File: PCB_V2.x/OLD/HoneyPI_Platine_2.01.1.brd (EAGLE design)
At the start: 80 x 100 mm, 89 parts

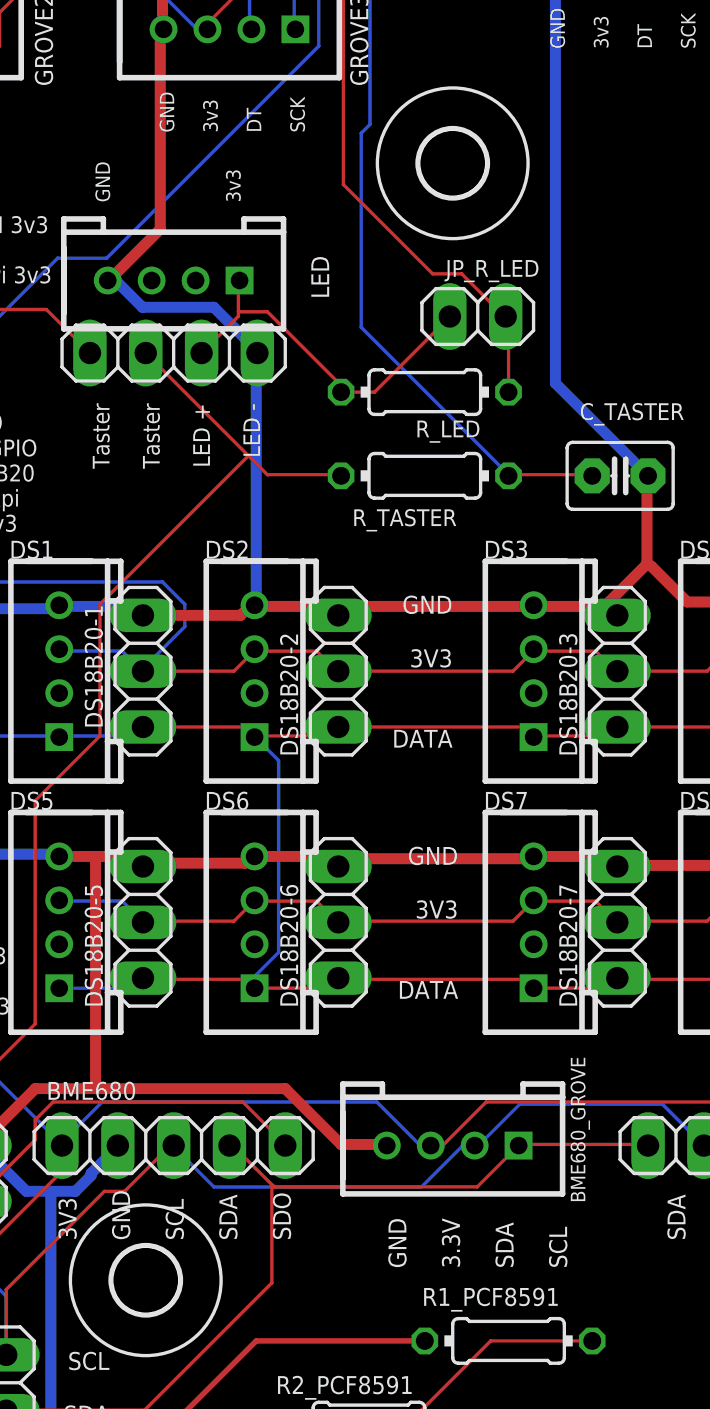
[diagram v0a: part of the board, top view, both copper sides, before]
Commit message: New releases
Fix BME680_GROVE Pinout on the main board
Some corrections on the sensor board
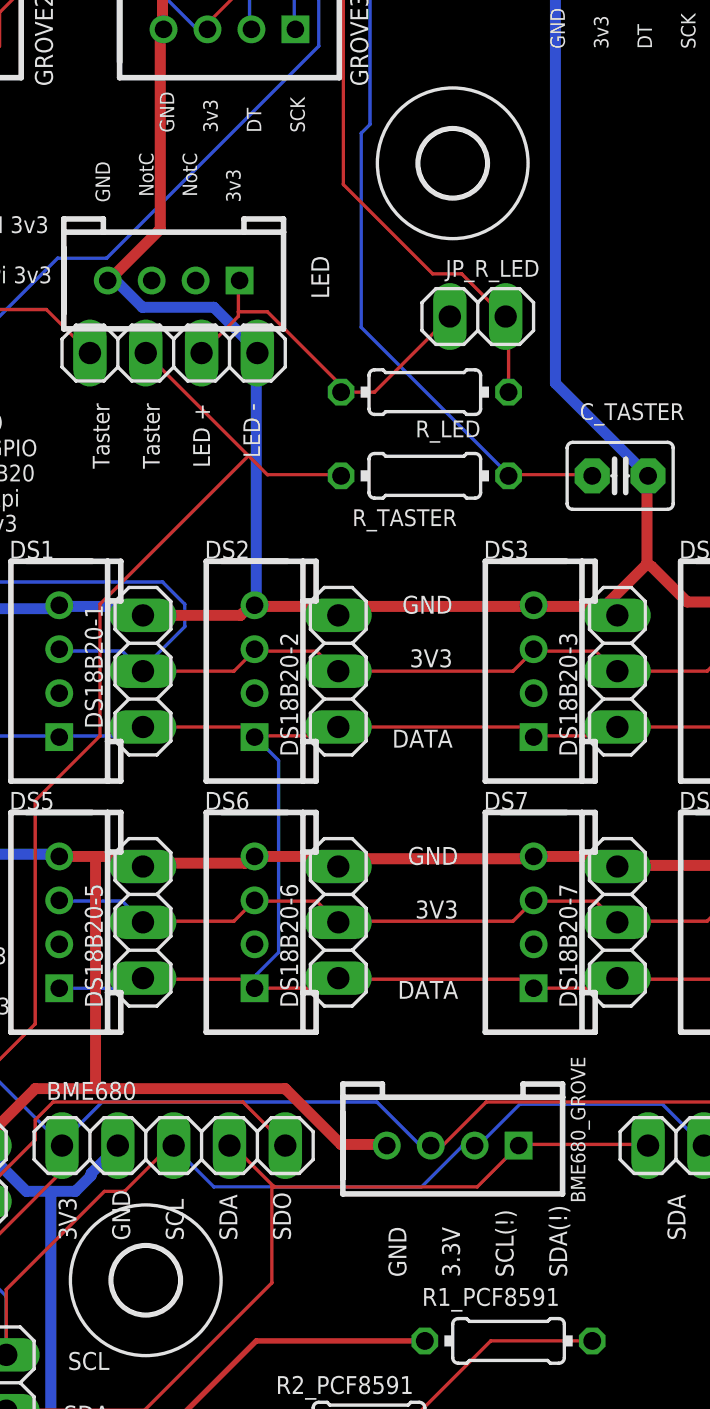
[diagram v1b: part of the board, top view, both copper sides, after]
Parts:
- C_SP1: value 100µF -> xxµF
- C_SP2: value 1µF -> xµF
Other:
- board text added: "GND 3.3V SCL(!) SDA(!)"
- board text added: "GND NotC NotC 3v3"
- board text removed: "GND 3.3V SDA SCL"
- board text removed: "GND 3v3"
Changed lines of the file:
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@@
 <drawing>
 <settings>
-<setting alwaysvectorfont="yes"/>
+<setting alwaysvectorfont="no"/>
 <setting verticaltext="up"/>
 </settings>
@@
 </layers>
 <board>
-<fusionsync huburn="a.cGVyc29uYWw6dWUyYjlkYjlm" projecturn="a.cGVyc29uYWw6dWUyYjlkYjlmIzIwMTcwNDEzNzE3MzExMDE" f3durn="urn:adsk.wipprod:dm.lineage:GkcBSzvJT7K4Bick1Iit8w" pcbguid="" lastpulledtime="" lastsyncedchangeguid="" latestrevisionid="f7b36f48-5fd6-4382-b252-79246711c0d3" lastsyncedrevisionid="f7b36f48-5fd6-4382-b252-79246711c0d3" lastboardhashguid="1bca5865-5669-4ab1-a0ca-56b80251d355" lastpushedtime="2020-06-08T22:28:48Z" linktopcb3d="true"/>
+<fusionsync huburn="a.cGVyc29uYWw6dWUyYjlkYjlm" projecturn="a.cGVyc29uYWw6dWUyYjlkYjlmIzIwMTcwNDEzNzE3MzExMDE" f3durn="urn:adsk.wipprod:dm.lineage:GkcBSzvJT7K4Bick1Iit8w" pcbguid="" lastpulledtime="" lastsyncedchangeguid="" latestrevisionid="f7b36f48-5fd6-4382-b252-79246711c0d3" lastsyncedrevisionid="f7b36f48-5fd6-4382-b252-79246711c0d3" lastboardhashguid="1bca5865-5669-4ab1-a0ca-56b80251d355" lastpushedtime="2020-06-08T22:28:48Z" linktopcb3d="false"/>
 <plain>
 <wire x1="0" y1="0" x2="80" y2="0" width="0" layer="20"/>
@@
 <wire x1="0" y1="100" x2="0" y2="0" width="0" layer="20"/>
 <hole x="2.54" y="94.234" drill="3" locked="yes" grouprefs="RASPBERRY"/>
-<hole x="2.54" y="71.374" drill="3" grouprefs="RASPBERRY HX711_1"/>
+<hole x="2.54" y="71.374" drill="3" grouprefs="HX711_1 RASPBERRY"/>
 <text x="13.843" y="77.216" size="0.8128" layer="25" rot="R180" grouprefs="HX711_1">3V3
 (DT/DAT)
@@
 SCK</text>
 <text x="51.308" y="69.596" size="0.6604" layer="25" rot="R90">GND
+ NotC
+ NotC
 3v3</text>
 <text x="37.973" y="64.77" size="0.762" layer="25">PIN3
@@
 GND</text>
 <hole x="77.47" y="20.54" drill="3"/>
-<text x="66.167" y="21.082" size="0.8128" layer="25" rot="R90">GND
+<text x="66.167" y="20.682" size="0.8128" layer="25" rot="R90">GND
 3.3V
-SDA
-SCL
+SCL(!)
+SDA(!)
 </text>
 <hole x="2.54" y="52" drill="3"/>
@@
 <attribute name="VALUE" x="43.18" y="59.563" size="1.27" layer="27"/>
 </element>
-<element name="C_SP1" library="capacitor-wima" library_urn="urn:adsk.eagle:library:116" package="C2.5-3" package3d_urn="urn:adsk.eagle:package:5436/1" value="100µF" x="21.59" y="17.78" smashed="yes" rot="R270">
+<element name="C_SP1" library="capacitor-wima" library_urn="urn:adsk.eagle:library:116" package="C2.5-3" package3d_urn="urn:adsk.eagle:package:5436/1" value="xxµF" x="21.59" y="17.78" smashed="yes" rot="R270">
 <attribute name="NAME" x="23.368" y="19.431" size="0.8128" layer="25" ratio="10" rot="R270"/>
 <attribute name="POPULARITY" value="38" x="21.59" y="16.51" size="0.8128" layer="27" rot="R270" display="off"/>
 <attribute name="VALUE" x="18.542" y="19.431" size="0.8128" layer="27" ratio="10" rot="R270"/>
 </element>
-<element name="C_SP2" library="capacitor-wima" library_urn="urn:adsk.eagle:library:116" package="C2.5-3" package3d_urn="urn:adsk.eagle:package:5436/1" value="1µF" x="21.59" y="25.4" smashed="yes" rot="R270">
+<element name="C_SP2" library="capacitor-wima" library_urn="urn:adsk.eagle:library:116" package="C2.5-3" package3d_urn="urn:adsk.eagle:package:5436/1" value="xµF" x="21.59" y="25.4" smashed="yes" rot="R270">
 <attribute name="NAME" x="23.368" y="27.051" size="0.8128" layer="25" ratio="10" rot="R270"/>
 <attribute name="POPULARITY" value="38" x="21.59" y="26.67" size="0.8128" layer="27" rot="R270" display="off"/>
